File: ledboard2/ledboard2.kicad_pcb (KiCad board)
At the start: 2 copper layers, 108 parts, among them P1 CONN_01X03, P2 CONN_01X03, U1 NEOPIXEL, U10 NEOPIXEL, U100 NEOPIXEL, U11 NEOPIXEL, U12 NEOPIXEL, U13 NEOPIXEL, U14 NEOPIXEL, U15 NEOPIXEL, U16 NEOPIXEL, U17 NEOPIXEL, U18 NEOPIXEL, U19 NEOPIXEL, U2 NEOPIXEL, U20 NEOPIXEL, U21 NEOPIXEL, U22 NEOPIXEL, U23 NEOPIXEL, U24 NEOPIXEL, U25 NEOPIXEL, U26 NEOPIXEL, U27 NEOPIXEL, U28 NEOPIXEL, U29 NEOPIXEL, U3 NEOPIXEL, U30 NEOPIXEL, U31 NEOPIXEL, U32 NEOPIXEL, U33 NEOPIXEL, U34 NEOPIXEL, U35 NEOPIXEL, U36 NEOPIXEL, U37 NEOPIXEL, U38 NEOPIXEL, U39 NEOPIXEL, U4 NEOPIXEL, U40 NEOPIXEL, U41 NEOPIXEL, U42 NEOPIXEL, U43 NEOPIXEL, U44 NEOPIXEL, U45 NEOPIXEL, U46 NEOPIXEL, U47 NEOPIXEL, U48 NEOPIXEL, U49 NEOPIXEL, U5 NEOPIXEL, U50 NEOPIXEL, U51 NEOPIXEL, U52 NEOPIXEL, U53 NEOPIXEL, U54 NEOPIXEL, U55 NEOPIXEL, U56 NEOPIXEL, U57 NEOPIXEL, U58 NEOPIXEL, U59 NEOPIXEL, U6 NEOPIXEL, U60 NEOPIXEL, U61 NEOPIXEL, U62 NEOPIXEL, U63 NEOPIXEL, U64 NEOPIXEL, U65 NEOPIXEL, U66 NEOPIXEL, U67 NEOPIXEL, U68 NEOPIXEL, U69 NEOPIXEL, U7 NEOPIXEL, U70 NEOPIXEL, U71 NEOPIXEL, U72 NEOPIXEL, U73 NEOPIXEL, U74 NEOPIXEL, U75 NEOPIXEL, U76 NEOPIXEL, U77 NEOPIXEL, U78 NEOPIXEL, U79 NEOPIXEL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

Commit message: Move the board bits into the diagram borders.
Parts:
- moved U10 140.3 mm to (19.6, 178.4)
- moved U100 140.3 mm to (166.4, 178.4)
- moved U20 140.3 mm to (35.9, 178.4)
- moved U30 140.3 mm to (52.2, 178.4)
- moved U40 140.3 mm to (68.5, 178.4)
- moved U50 140.3 mm to (84.8, 178.4)
- moved U60 140.3 mm to (101.2, 178.4)
- moved U70 140.3 mm to (117.5, 178.4)
- moved U80 140.3 mm to (133.8, 178.4)
- moved U90 140.3 mm to (150.1, 178.4)
- moved U91 140.3 mm to (166.4, 31.6)
- moved U92 140.3 mm to (166.4, 47.9)
- moved U93 140.3 mm to (166.4, 64.2)
- moved U94 140.3 mm to (166.4, 80.5)
- moved U95 140.3 mm to (166.4, 96.8)
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
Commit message: Edge cuts
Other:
- board outline added: 161 x 170 mm
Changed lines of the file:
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@@
     (links 308)
     (no_connects 2)
-    (area -80.30119 -84.525001 78.025001 83.525001)
+    (area 12.222619 18.285 171.025001 188.525001)
     (thickness 1.6)
-    (drawings 0)
+    (drawings 10)
     (tracks 424)
     (zones 0)
@@
     (pad 1 thru_hole circle (at 0 0) (size 2 2) (drill 1.8) (layers *.Cu *.Mask F.SilkS))
   )
+  (gr_arc (start 171 188) (end 172 188) (angle 90) (layer Edge.Cuts) (width 0.1))
+  (gr_arc (start 13 187) (end 13 189) (angle 90) (layer Edge.Cuts) (width 0.1))
+  (gr_arc (start 13 21) (end 11 21) (angle 90) (layer Edge.Cuts) (width 0.1))
+  (gr_arc (start 170 21) (end 170 19) (angle 90) (layer Edge.Cuts) (width 0.1))
+  (gr_line (start 172 25) (end 172 21) (angle 90) (layer Edge.Cuts) (width 0.1))
+  (gr_line (start 13 19) (end 170 19) (angle 90) (layer Edge.Cuts) (width 0.1))
+  (gr_line (start 172 188) (end 172 25) (angle 90) (layer Edge.Cuts) (width 0.1))
+  (gr_line (start 11 187) (end 11 183) (angle 90) (layer Edge.Cuts) (width 0.1))
+  (gr_line (start 171 189) (end 13 189) (angle 90) (layer Edge.Cuts) (width 0.1))
+  (gr_line (start 11 21) (end 11 183) (angle 90) (layer Edge.Cuts) (width 0.1))
   (segment (start 19.54 25.5) (end 19.54 28.812569) (width 0.5) (layer B.Cu) (net 1))
   (segment (start 19.54 28.812569) (end 18.9495 29.403069) (width 0.5) (layer B.Cu) (net 1))

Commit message: Final tweaks before ordering v0.1 PCBs.
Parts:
- R1: moved to B.Cu
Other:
- board text added: "Wordclock v0.1"
- board text added: "https://github.com/apparentlymart/wordclock"
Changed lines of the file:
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@@
     (links 308)
     (no_connects 2)
-    (area 12.222619 18.285 171.025001 188.525001)
+    (area 10.146429 18.285 172.050001 189.050001)
     (thickness 1.6)
-    (drawings 10)
-    (tracks 424)
+    (drawings 12)
+    (tracks 425)
     (zones 0)
     (modules 108)
@@
     (visible_elements FFFFFF7F)
     (pcbplotparams
-      (layerselection 0x00000_80000000)
-      (usegerberextensions false)
+      (layerselection 0x010fc_80000001)
+      (usegerberextensions true)
       (excludeedgelayer true)
       (linewidth 0.100000)
@@
       (padsonsilk false)
       (subtractmaskfromsilk false)
-      (outputformat 3)
+      (outputformat 1)
       (mirror false)
-      (drillshape 1)
+      (drillshape 0)
       (scaleselection 1)
       (outputdirectory ""))
@@
     )
   )
-  (module Resistors_SMD:R_0805_HandSoldering (layer F.Cu)
+  (module Resistors_SMD:R_0805_HandSoldering (layer B.Cu)
     (at 14 31.5 90)
     (descr "Resistor SMD 0805, hand soldering")
     (tags "resistor 0805")
     (attr smd)
-    (fp_text reference R1 (at -3.5 0 90) (layer F.SilkS)
-      (effects (font (size 1 1) (thickness 0.15)))
-    )
-    (fp_text value 300 (at 0 2.1 90) (layer F.Fab)
-      (effects (font (size 1 1) (thickness 0.15)))
-    )
-    (fp_line (start -2.4 -1) (end 2.4 -1) (layer F.CrtYd) (width 0.05))
-    (fp_line (start -2.4 1) (end 2.4 1) (layer F.CrtYd) (width 0.05))
-    (fp_line (start -2.4 -1) (end -2.4 1) (layer F.CrtYd) (width 0.05))
-    (fp_line (start 2.4 -1) (end 2.4 1) (layer F.CrtYd) (width 0.05))
-    (fp_line (start 0.6 0.875) (end -0.6 0.875) (layer F.SilkS) (width 0.15))
-    (fp_line (start -0.6 -0.875) (end 0.6 -0.875) (layer F.SilkS) (width 0.15))
-    (pad 1 smd rect (at -1.35 0 90) (size 1.5 1.3) (layers F.Cu F.Paste F.Mask)
+    (fp_text reference R1 (at -3.5 0 90) (layer B.SilkS)
+      (effects (font (size 1 1) (thickness 0.15)) (justify mirror))
+    )
+    (fp_text value 300 (at 0 -2.1 90) (layer B.Fab)
+      (effects (font (size 1 1) (thickness 0.15)) (justify mirror))
+    )
+    (fp_line (start -2.4 1) (end 2.4 1) (layer B.CrtYd) (width 0.05))
+    (fp_line (start -2.4 -1) (end 2.4 -1) (layer B.CrtYd) (width 0.05))
+    (fp_line (start -2.4 1) (end -2.4 -1) (layer B.CrtYd) (width 0.05))
+    (fp_line (start 2.4 1) (end 2.4 -1) (layer B.CrtYd) (width 0.05))
+    (fp_line (start 0.6 -0.875) (end -0.6 -0.875) (layer B.SilkS) (width 0.15))
+    (fp_line (start -0.6 0.875) (end 0.6 0.875) (layer B.SilkS) (width 0.15))
+    (pad 1 smd rect (at -1.35 0 90) (size 1.5 1.3) (layers B.Cu B.Paste B.Mask)
       (net 5 "Net-(R1-Pad1)"))
-    (pad 2 smd rect (at 1.35 0 90) (size 1.5 1.3) (layers F.Cu F.Paste F.Mask)
+    (pad 2 smd rect (at 1.35 0 90) (size 1.5 1.3) (layers B.Cu B.Paste B.Mask)
       (net 4 DIN))
     (model Resistors_SMD.3dshapes/R_0805_HandSoldering.wrl
@@
     )
     (pad 1 thru_hole circle (at 0 0) (size 2 2) (drill 1.8) (layers *.Cu *.Mask F.SilkS))
+  )
+  (gr_text https://github.com/apparentlymart/wordclock (at 170 23) (layer F.SilkS)
+    (effects (font (size 1 1) (thickness 0.25)) (justify right))
+  )
+  (gr_text "Wordclock v0.1" (at 170 21) (layer F.SilkS)
+    (effects (font (size 1.5 1.5) (thickness 0.3)) (justify right))
   )
   (gr_arc (start 171 188) (end 172 188) (angle 90) (layer Edge.Cuts) (width 0.1))
@@
   (segment (start 169 184) (end 169 186.5) (width 0.25) (layer F.Cu) (net 3))
   (segment (start 168.3255 183.3255) (end 169 184) (width 0.25) (layer F.Cu) (net 3))
-  (segment (start 17 25.5) (end 17 27.15) (width 0.25) (layer F.Cu) (net 4))
-  (segment (start 17 27.15) (end 14 30.15) (width 0.25) (layer F.Cu) (net 4))
-  (segment (start 14 32.85) (end 16.4115 32.85) (width 0.25) (layer F.Cu) (net 5))
-  (segment (start 16.4115 32.85) (end 17.6745 31.587) (width 0.25) (layer F.Cu) (net 5))
+  (segment (start 17 25.5) (end 16.5 25.5) (width 0.25) (layer B.Cu) (net 4))
+  (segment (start 16.5 25.5) (end 14 28) (width 0.25) (layer B.Cu) (net 4))
+  (segment (start 14 28) (end 14 30.15) (width 0.25) (layer B.Cu) (net 4))
+  (segment (start 14 32.85) (end 16.4115 32.85) (width 0.25) (layer B.Cu) (net 5))
+  (segment (start 16.4115 32.85) (end 17.6745 31.587) (width 0.25) (layer B.Cu) (net 5))
   (segment (start 21.4995 31.587) (end 33.9885 31.587) (width 0.25) (layer F.Cu) (net 6))
   (segment (start 21.4995 47.901) (end 33.9885 47.901) (width 0.25) (layer F.Cu) (net 7))

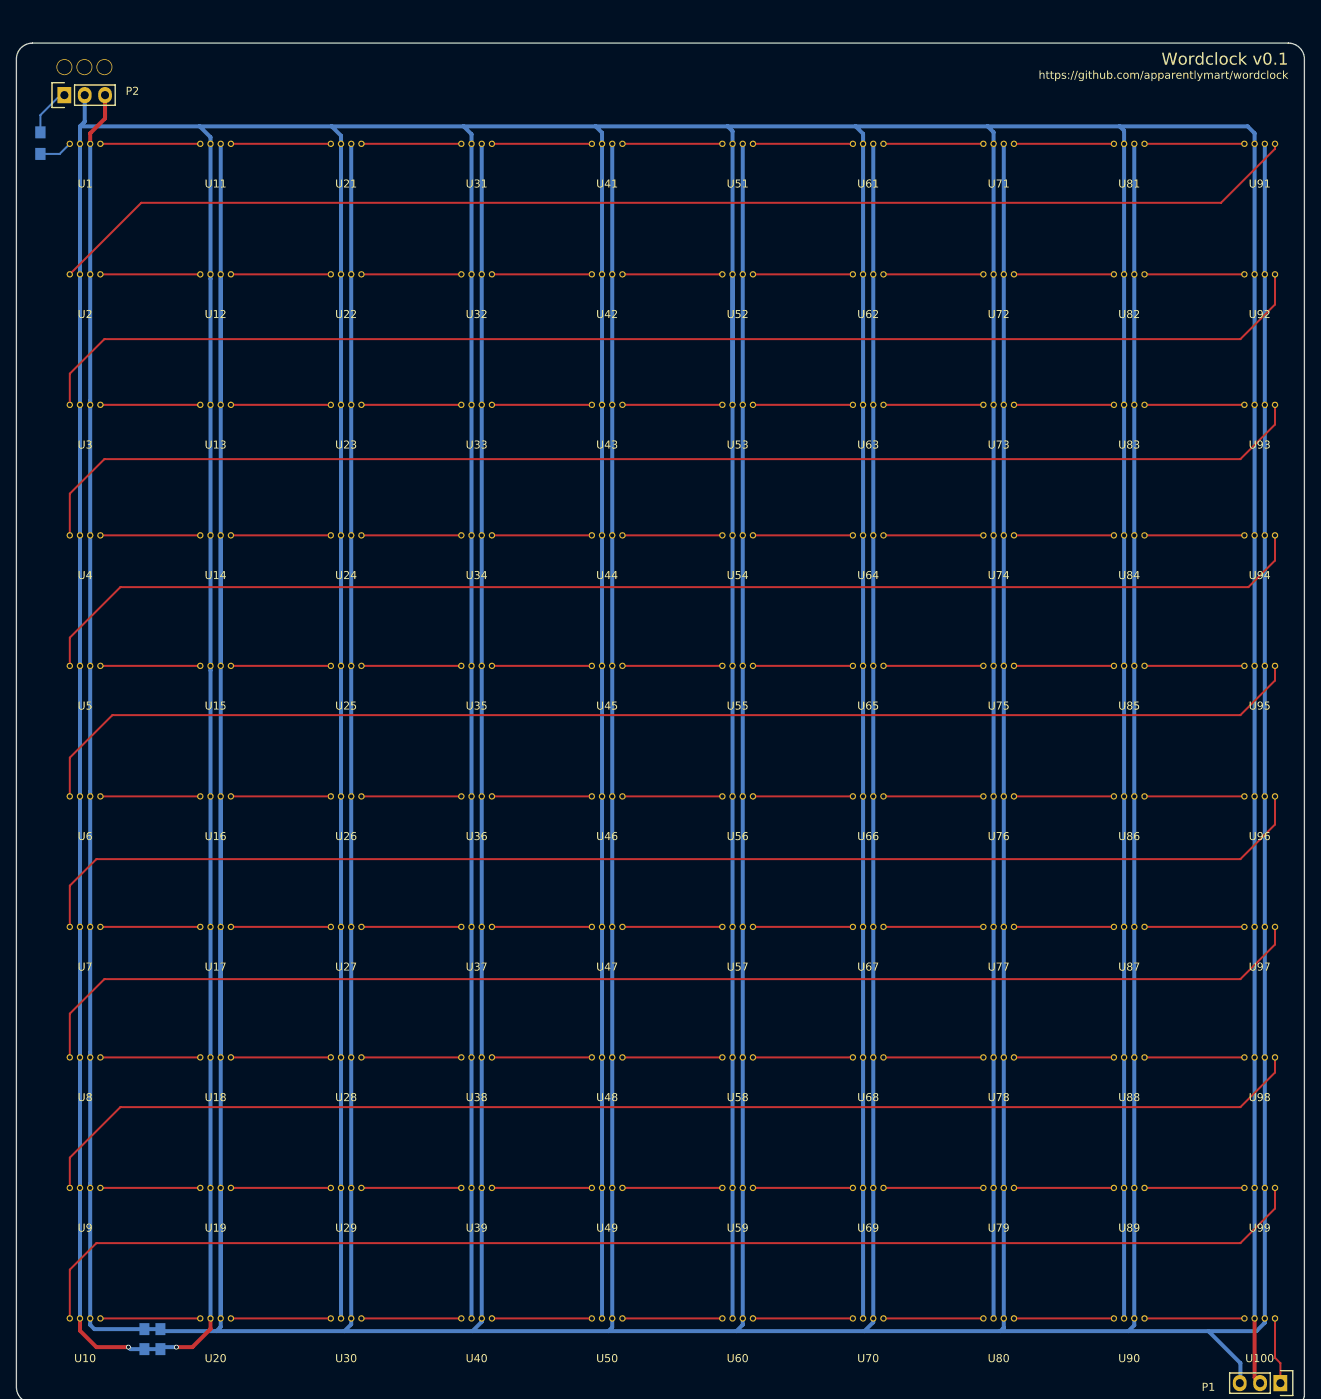
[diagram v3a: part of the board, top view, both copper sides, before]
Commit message: Increase NeoPixel hole sizes and add bigger capacitor.
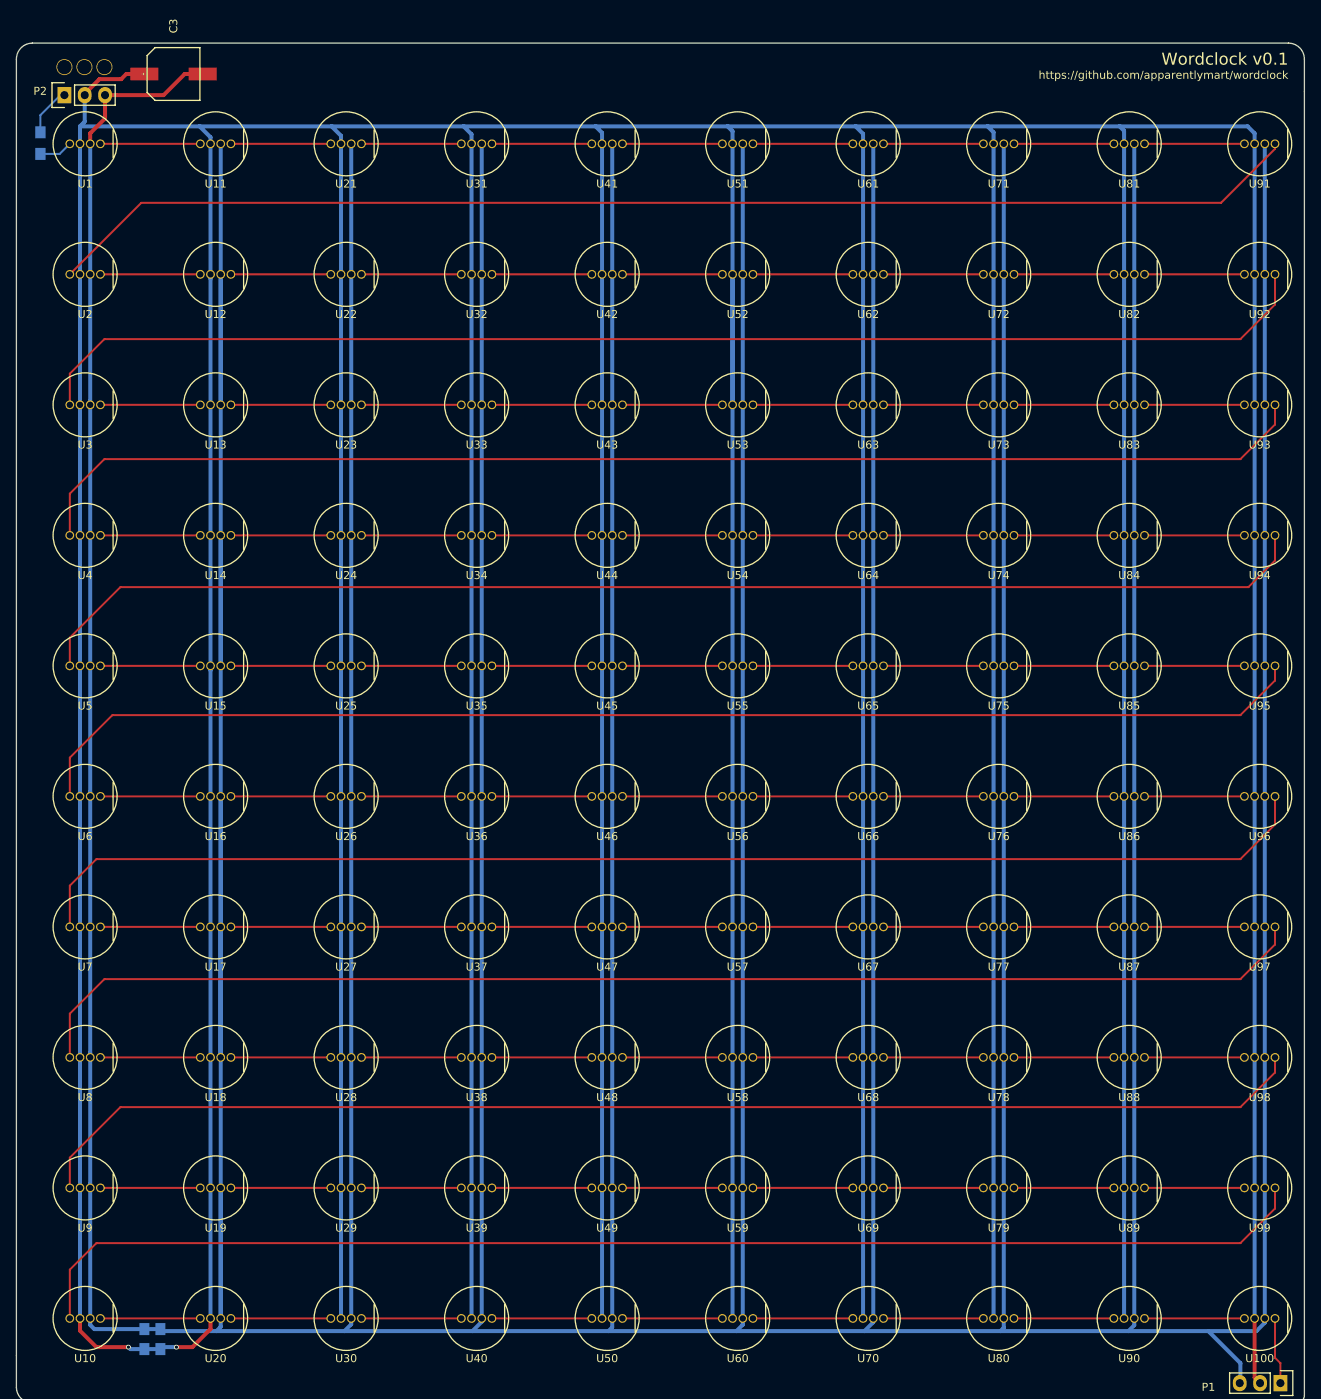
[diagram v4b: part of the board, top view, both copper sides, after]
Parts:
- added C3: CP, ledboard2:CPOL_SMD_6.3mm, F.Cu at (30.6, 22.9)
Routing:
- net GND: track 1746.0 -> 1759.3 mm
- net +5V: track 1690.0 -> 1698.6 mm
